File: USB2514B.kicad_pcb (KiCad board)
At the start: 4 copper layers, 76 parts, among them J1 USB_A, J2 USB_C_Receptacle_USB2.0_16P, J3 USB_A, J4 USB_A, J6 USB_A, U1 USB2514B_Bi, U10 USBLC6-2P6, U11 USBLC6-2P6, U2 USBLC6-2P6, U3 AP22615AWU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

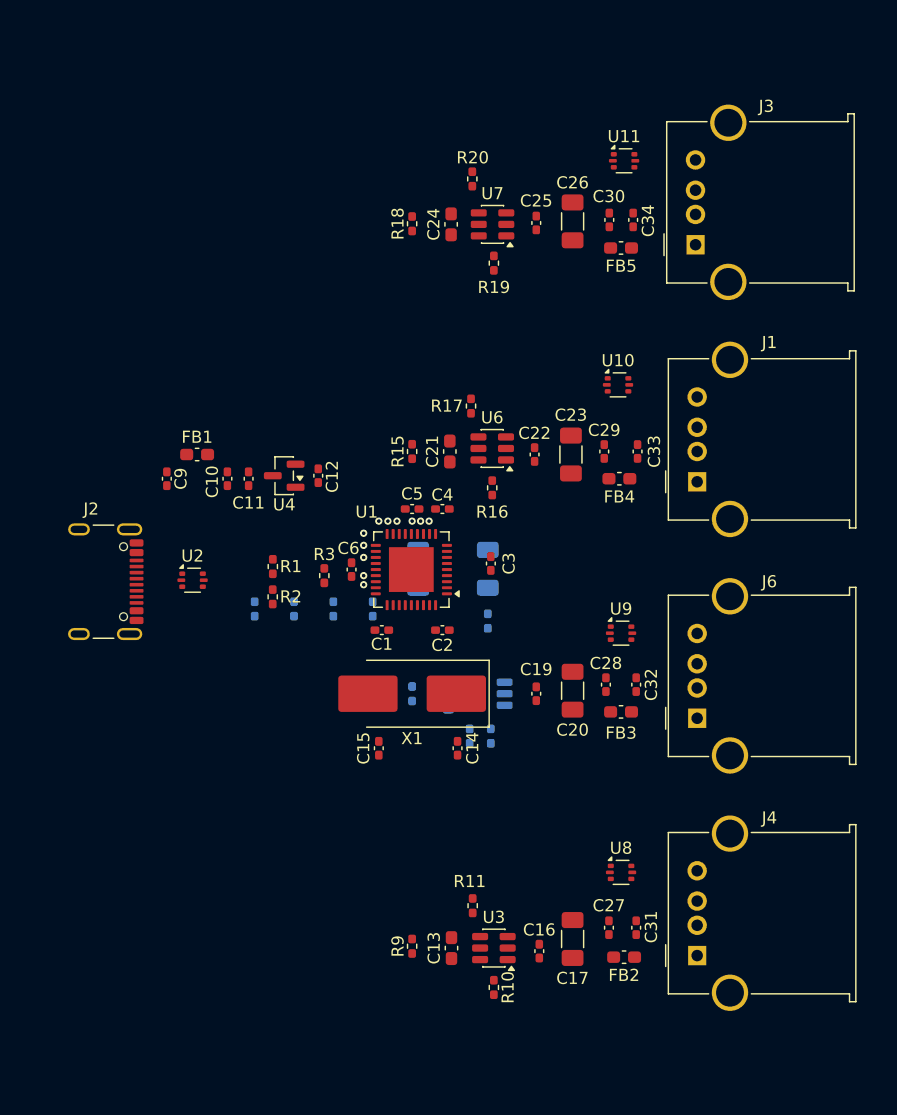
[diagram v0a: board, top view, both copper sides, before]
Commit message: Added board outline via Edge.Cuts traces
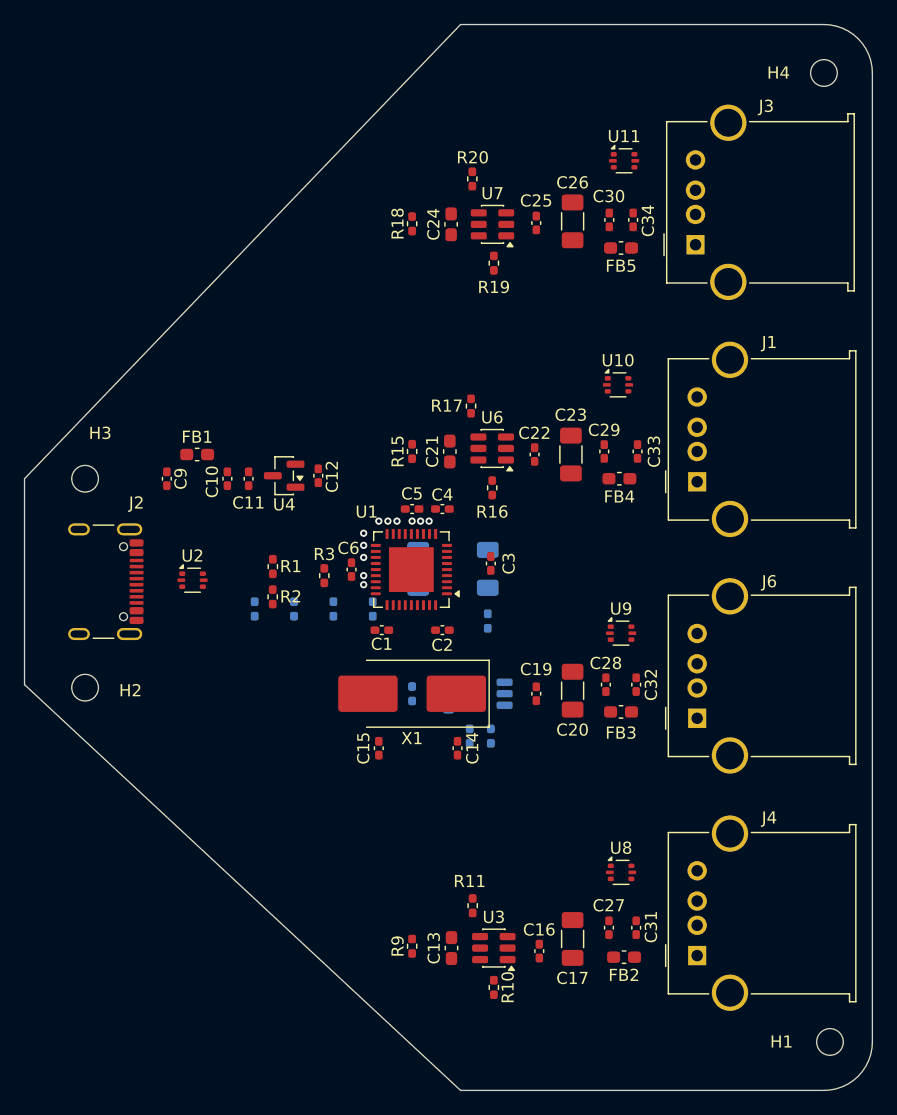
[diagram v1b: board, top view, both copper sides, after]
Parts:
- added H1: MountingHole, MountingHole:MountingHole_2.2mm_M2, F.Cu at (186.5, 149.5)
- added H2: MountingHole, MountingHole:MountingHole_2.2mm_M2, F.Cu at (125.0, 120.2)
- added H3: MountingHole, MountingHole:MountingHole_2.2mm_M2, F.Cu at (125.0, 103.0)
- added H4: MountingHole, MountingHole:MountingHole_2.2mm_M2, F.Cu at (186.0, 69.5)
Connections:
- net /D+_DN1 renamed /D_DN1+
- net /D+_DN2 renamed /D_DN2+
- net /D+_DN3 renamed /D_DN3+
- net /D+_DN4 renamed /D_DN4+
- net /D-_DN1 renamed /D_DN1-
- net /D-_DN2 renamed /D_DN2-
- net /D-_DN3 renamed /D_DN3-
- net /D-_DN4 renamed /D_DN4-
- J2 pad A6: Net-(J2-D+-PadA6) -> /D_UP+
- J2 pad A7: Net-(J2-D--PadA7) -> /D_UP-
- J2 pad B6: Net-(J2-D+-PadA6) -> /D_UP+
- J2 pad B7: Net-(J2-D--PadA7) -> /D_UP-
- U1 pad 30: /D+_UP -> /D_UP-
- U1 pad 31: /D-_UP -> /D_UP+
- U2 pad 1: Net-(J2-D--PadA7) -> /D_UP-
- U2 pad 3: Net-(J2-D+-PadA6) -> /D_UP+
- U2 pad 4: /D-_UP -> /D_UP+
- U2 pad 6: /D+_UP -> /D_UP-
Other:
- board outline added: 70 x 88 mm
